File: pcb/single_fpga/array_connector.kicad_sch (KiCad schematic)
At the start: 1 part, among them J2 AXK680337YG

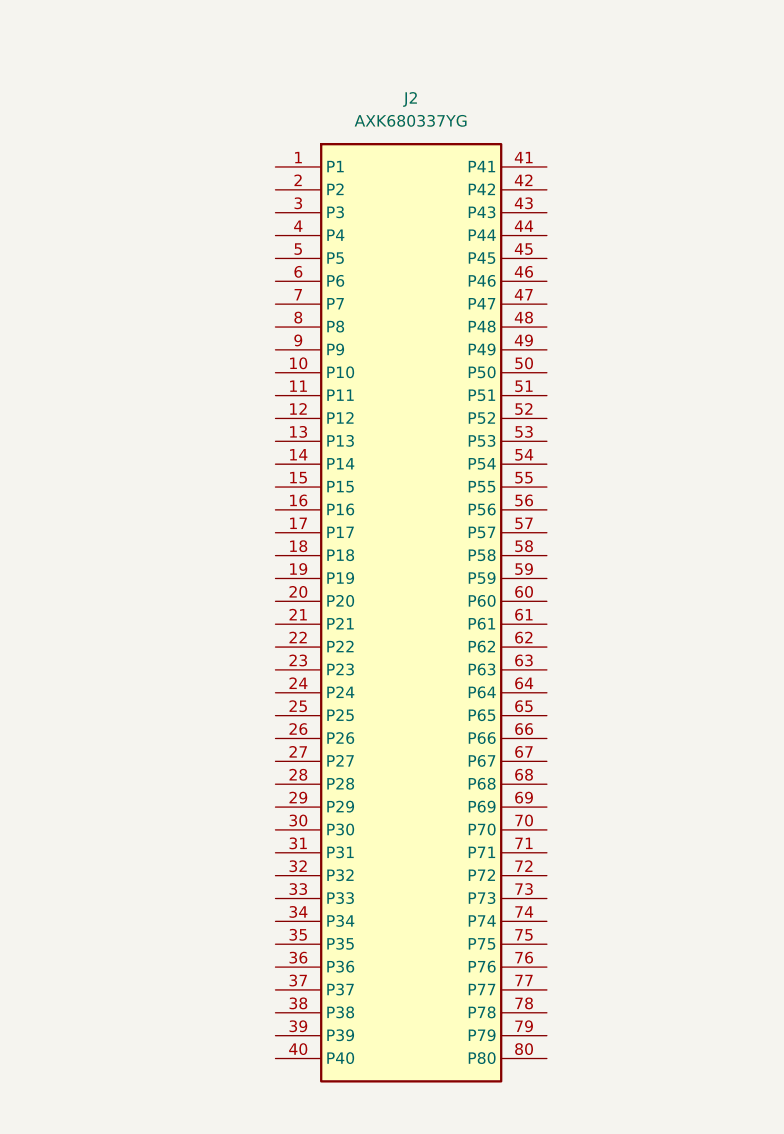
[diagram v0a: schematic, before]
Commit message: Reorganized sheets for two-boards. Fixed connector off-grid problems.
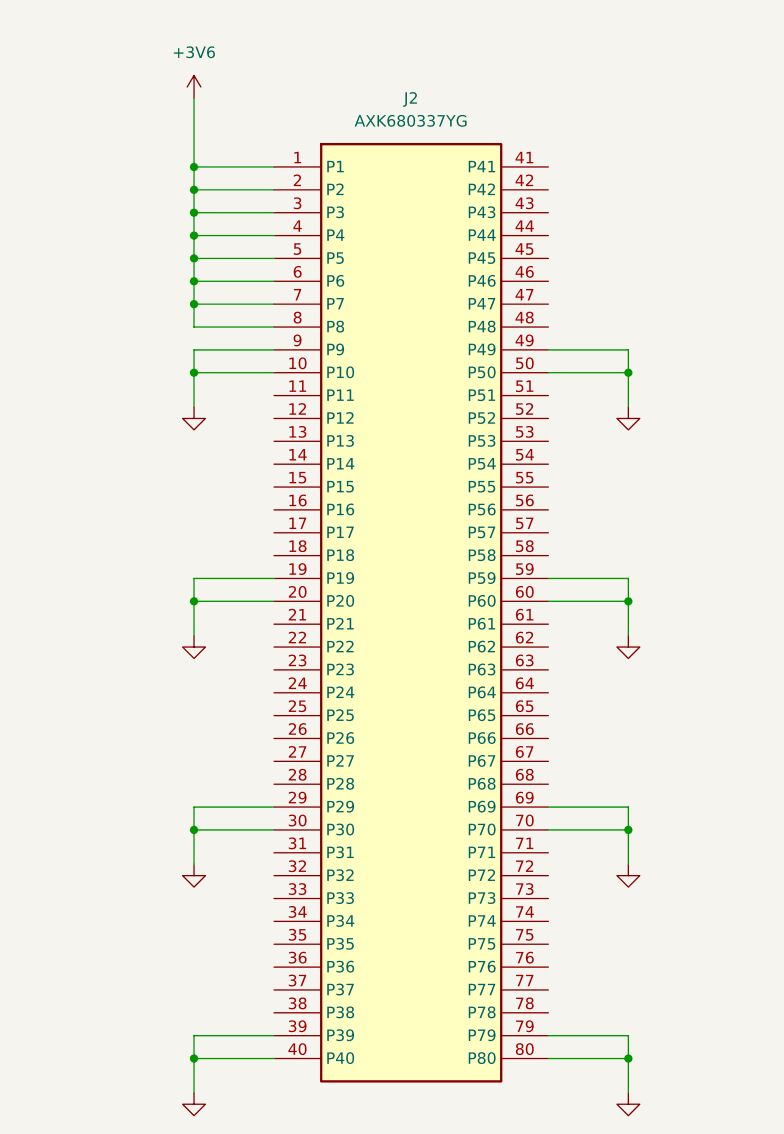
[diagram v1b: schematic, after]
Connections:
- net +3V6: now reaches J2.1 (P1)
- net +3V6: now also J2.2 (P2), J2.3 (P3), J2.4 (P4), J2.5 (P5), J2.6 (P6), J2.7 (P7), J2.8 (P8)
- net GND: now reaches J2.10 (P10)
- net GND: now also J2.19 (P19), J2.20 (P20), J2.29 (P29), J2.30 (P30), J2.39 (P39), J2.40 (P40), J2.49 (P49), J2.50 (P50), J2.59 (P59), J2.60 (P60), J2.69 (P69), J2.70 (P70), J2.79 (P79), J2.80 (P80), J2.9 (P9)

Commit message: Fixed another off-grid issue. Connected power and DATA_?? pins to inter-board connector.
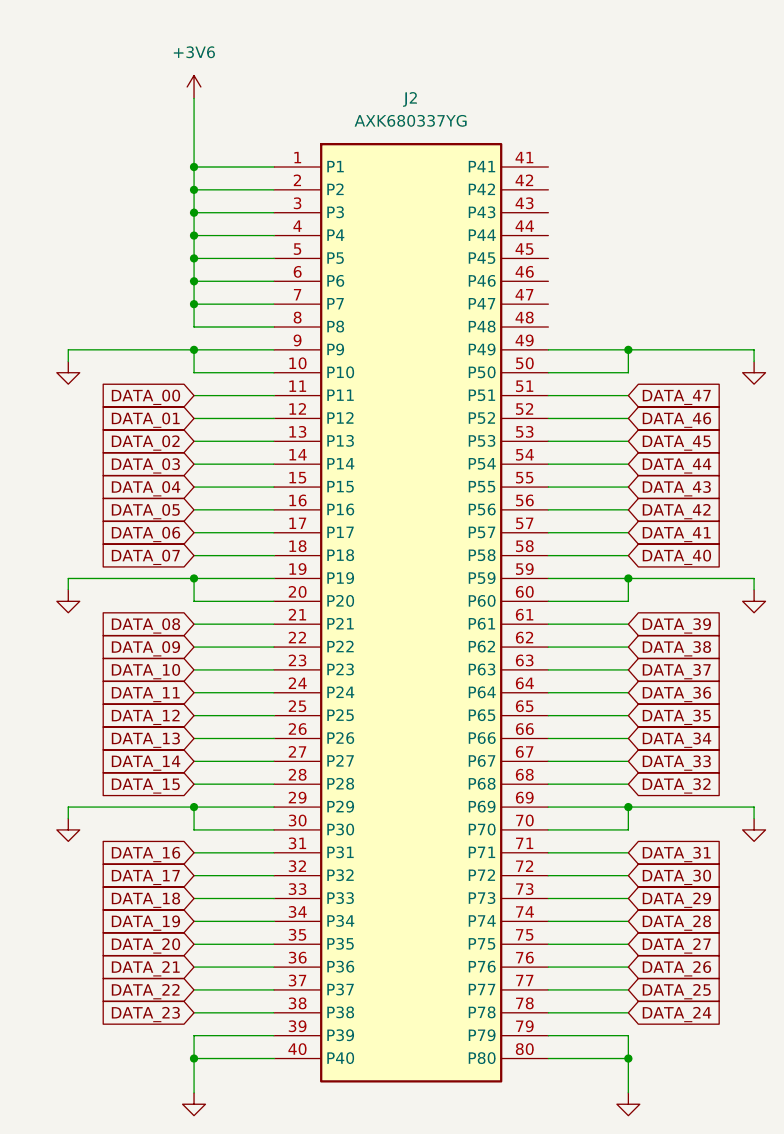
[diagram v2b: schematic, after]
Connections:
- net DATA_00: now reaches J2.11 (P11)
- net DATA_01: now reaches J2.12 (P12)
- net DATA_02: now reaches J2.13 (P13)
- net DATA_03: now reaches J2.14 (P14)
- net DATA_04: now reaches J2.15 (P15)
- net DATA_05: now reaches J2.16 (P16)
- net DATA_06: now reaches J2.17 (P17)
- net DATA_07: now reaches J2.18 (P18)
- net DATA_08: now reaches J2.21 (P21)
- net DATA_09: now reaches J2.22 (P22)
- net DATA_10: now reaches J2.23 (P23)
- net DATA_11: now reaches J2.24 (P24)
- net DATA_12: now reaches J2.25 (P25)
- net DATA_13: now reaches J2.26 (P26)
- net DATA_14: now reaches J2.27 (P27)
- net DATA_15: now reaches J2.28 (P28)
- net DATA_16: now reaches J2.31 (P31)
- net DATA_17: now reaches J2.32 (P32)
- net DATA_18: now reaches J2.33 (P33)
- net DATA_19: now reaches J2.34 (P34)
- net DATA_20: now reaches J2.35 (P35)
- net DATA_21: now reaches J2.36 (P36)
- net DATA_22: now reaches J2.37 (P37)
- net DATA_23: now reaches J2.38 (P38)
- net DATA_47: now reaches J2.51 (P51)
- net DATA_46: now reaches J2.52 (P52)
- net DATA_45: now reaches J2.53 (P53)
- net DATA_44: now reaches J2.54 (P54)
- net DATA_43: now reaches J2.55 (P55)
- net DATA_42: now reaches J2.56 (P56)
- net DATA_41: now reaches J2.57 (P57)
- net DATA_40: now reaches J2.58 (P58)
- net DATA_39: now reaches J2.61 (P61)
- net DATA_38: now reaches J2.62 (P62)
- net DATA_37: now reaches J2.63 (P63)
- net DATA_36: now reaches J2.64 (P64)
- net DATA_35: now reaches J2.65 (P65)
- net DATA_34: now reaches J2.66 (P66)
- net DATA_33: now reaches J2.67 (P67)
- net DATA_32: now reaches J2.68 (P68)
- net DATA_31: now reaches J2.71 (P71)
- net DATA_30: now reaches J2.72 (P72)
- net DATA_29: now reaches J2.73 (P73)
- net DATA_28: now reaches J2.74 (P74)
- net DATA_27: now reaches J2.75 (P75)
- net DATA_26: now reaches J2.76 (P76)
- net DATA_25: now reaches J2.77 (P77)
- net DATA_24: now reaches J2.78 (P78)

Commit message: Updated all refdes's.
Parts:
- renumbered J2 to J1
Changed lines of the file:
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@@
 		(dnp no)
 		(fields_autoplaced yes)
-		(property "Reference" "#PWR0485"
+		(property "Reference" "#PWR043"
 			(at 176.53 99.06 0)
 			(hide yes)
@@
 			(project "top"
 				(path "/12638caa-1907-413e-8e98-06abbbf6ccbc/518a49d4-764a-4074-9d90-4928dda6bfa7/a249d55d-7359-47b8-9860-fb25b30b5b2a"
-					(reference "#PWR0485")
+					(reference "#PWR043")
 					(unit 1)
 				)
@@
 		(dnp no)
 		(fields_autoplaced yes)
-		(property "Reference" "#PWR0481"
+		(property "Reference" "#PWR037"
 			(at 100.33 99.06 0)
 			(hide yes)
@@
 			(project "top"
 				(path "/12638caa-1907-413e-8e98-06abbbf6ccbc/518a49d4-764a-4074-9d90-4928dda6bfa7/a249d55d-7359-47b8-9860-fb25b30b5b2a"
-					(reference "#PWR0481")
+					(reference "#PWR037")
 					(unit 1)
 				)
@@
 		(dnp no)
 		(fields_autoplaced yes)
-		(property "Reference" "#PWR0482"
+		(property "Reference" "#PWR038"
 			(at 100.33 124.46 0)
 			(hide yes)
@@
 			(project "top"
 				(path "/12638caa-1907-413e-8e98-06abbbf6ccbc/518a49d4-764a-4074-9d90-4928dda6bfa7/a249d55d-7359-47b8-9860-fb25b30b5b2a"
-					(reference "#PWR0482")
+					(reference "#PWR038")
 					(unit 1)
 				)
@@
 		(dnp no)
 		(fields_autoplaced yes)
-		(property "Reference" "#PWR0480"
+		(property "Reference" "#PWR036"
 			(at 100.33 73.66 0)
 			(hide yes)
@@
 			(project "top"
 				(path "/12638caa-1907-413e-8e98-06abbbf6ccbc/518a49d4-764a-4074-9d90-4928dda6bfa7/a249d55d-7359-47b8-9860-fb25b30b5b2a"
-					(reference "#PWR0480")
+					(reference "#PWR036")
 					(unit 1)
 				)
@@
 		(dnp no)
 		(fields_autoplaced yes)
-		(property "Reference" "J2"
+		(property "Reference" "J1"
 			(at 138.43 38.1 0)
 			(show_name no)
@@
 			(project "top"
 				(path "/12638caa-1907-413e-8e98-06abbbf6ccbc/518a49d4-764a-4074-9d90-4928dda6bfa7/a249d55d-7359-47b8-9860-fb25b30b5b2a"
-					(reference "J2")
+					(reference "J1")
 					(unit 1)
 				)
@@
 		(dnp no)
 		(fields_autoplaced yes)
-		(property "Reference" "#PWR0483"
+		(property "Reference" "#PWR040"
 			(at 114.3 154.94 0)
 			(hide yes)
@@
 			(project "top"
 				(path "/12638caa-1907-413e-8e98-06abbbf6ccbc/518a49d4-764a-4074-9d90-4928dda6bfa7/a249d55d-7359-47b8-9860-fb25b30b5b2a"
-					(reference "#PWR0483")
+					(reference "#PWR040")
 					(unit 1)
 				)
@@
 		(dnp no)
 		(fields_autoplaced yes)
-		(property "Reference" "#PWR0486"
+		(property "Reference" "#PWR044"
 			(at 176.53 124.46 0)
 			(hide yes)
@@
 			(project "top"
 				(path "/12638caa-1907-413e-8e98-06abbbf6ccbc/518a49d4-764a-4074-9d90-4928dda6bfa7/a249d55d-7359-47b8-9860-fb25b30b5b2a"
-					(reference "#PWR0486")
+					(reference "#PWR044")
 					(unit 1)
 				)
@@
 		(dnp no)
 		(fields_autoplaced yes)
-		(property "Reference" "#PWR0484"
+		(property "Reference" "#PWR042"
 			(at 176.53 73.66 0)
 			(hide yes)
@@
 			(project "top"
 				(path "/12638caa-1907-413e-8e98-06abbbf6ccbc/518a49d4-764a-4074-9d90-4928dda6bfa7/a249d55d-7359-47b8-9860-fb25b30b5b2a"
-					(reference "#PWR0484")
+					(reference "#PWR042")
 					(unit 1)
 				)
@@
 		(dnp no)
 		(fields_autoplaced yes)
-		(property "Reference" "#PWR0495"
+		(property "Reference" "#PWR039"
 			(at 114.3 41.91 0)
 			(hide yes)
@@
 			(project "top"
 				(path "/12638caa-1907-413e-8e98-06abbbf6ccbc/518a49d4-764a-4074-9d90-4928dda6bfa7/a249d55d-7359-47b8-9860-fb25b30b5b2a"
-					(reference "#PWR0495")
+					(reference "#PWR039")
 					(unit 1)
 				)
@@
 		(dnp no)
 		(fields_autoplaced yes)
-		(property "Reference" "#PWR0487"
+		(property "Reference" "#PWR041"
 			(at 162.56 154.94 0)
 			(hide yes)
@@
 			(project "top"
 				(path "/12638caa-1907-413e-8e98-06abbbf6ccbc/518a49d4-764a-4074-9d90-4928dda6bfa7/a249d55d-7359-47b8-9860-fb25b30b5b2a"
-					(reference "#PWR0487")
+					(reference "#PWR041")
 					(unit 1)
 				)

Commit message: Changed inter-board connectors (J1 and J2) to be taller.
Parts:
- J1: value AXK680337YG -> AXK6S80347YG; footprint single_fpga:AXK680337YG -> AXK6S80347YG:CONN80_AXK6S80347YG_PAN; symbol AXK680337YG:AXK680337YG -> AXK6S80347YG:AXK6S80347YG
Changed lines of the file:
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@@
 	)
 	(symbol
-		(lib_id "AXK680337YG:AXK680337YG")
+		(lib_id "AXK6S80347YG:AXK6S80347YG")
 		(at 138.43 95.25 0)
 		(unit 1)
@@
 			)
 		)
-		(property "Value" "AXK680337YG"
+		(property "Value" "AXK6S80347YG"
 			(at 138.43 40.64 0)
 			(show_name no)
@@
 			)
 		)
-		(property "Footprint" "single_fpga:AXK680337YG"
+		(property "Footprint" "AXK6S80347YG:CONN80_AXK6S80347YG_PAN"
 			(at 138.43 95.25 0)
 			(hide yes)

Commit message: Fixed power nets.
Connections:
- no-connect marks 0 -> 8
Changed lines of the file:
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@@
 		(color 0 0 0 0)
 	)
+	(no_connect
+		(at 153.67 55.88)
+	)
+	(no_connect
+		(at 153.67 63.5)
+	)
+	(no_connect
+		(at 153.67 53.34)
+	)
+	(no_connect
+		(at 153.67 45.72)
+	)
+	(no_connect
+		(at 153.67 48.26)
+	)
+	(no_connect
+		(at 153.67 58.42)
+	)
+	(no_connect
+		(at 153.67 50.8)
+	)
+	(no_connect
+		(at 153.67 60.96)
+	)
 	(wire
 		(pts
@@
 		)
 		(instances
-			(project "top"
-				(path "/12638caa-1907-413e-8e98-06abbbf6ccbc/518a49d4-764a-4074-9d90-4928dda6bfa7/a249d55d-7359-47b8-9860-fb25b30b5b2a"
+			(project "mic_array"
+				(path "/12638caa-1907-413e-8e98-06abbbf6ccbc/a249d55d-7359-47b8-9860-fb25b30b5b2a"
 					(reference "#PWR043")
 					(unit 1)
@@
 		)
 		(instances
-			(project "top"
-				(path "/12638caa-1907-413e-8e98-06abbbf6ccbc/518a49d4-764a-4074-9d90-4928dda6bfa7/a249d55d-7359-47b8-9860-fb25b30b5b2a"
+			(project "mic_array"
+				(path "/12638caa-1907-413e-8e98-06abbbf6ccbc/a249d55d-7359-47b8-9860-fb25b30b5b2a"
 					(reference "#PWR037")
 					(unit 1)
@@
 		)
 		(instances
-			(project "top"
-				(path "/12638caa-1907-413e-8e98-06abbbf6ccbc/518a49d4-764a-4074-9d90-4928dda6bfa7/a249d55d-7359-47b8-9860-fb25b30b5b2a"
+			(project "mic_array"
+				(path "/12638caa-1907-413e-8e98-06abbbf6ccbc/a249d55d-7359-47b8-9860-fb25b30b5b2a"
 					(reference "#PWR038")
 					(unit 1)
@@
 		)
 		(instances
-			(project "top"
-				(path "/12638caa-1907-413e-8e98-06abbbf6ccbc/518a49d4-764a-4074-9d90-4928dda6bfa7/a249d55d-7359-47b8-9860-fb25b30b5b2a"
+			(project "mic_array"
+				(path "/12638caa-1907-413e-8e98-06abbbf6ccbc/a249d55d-7359-47b8-9860-fb25b30b5b2a"
 					(reference "#PWR036")
 					(unit 1)
@@
 		)
 		(instances
-			(project "top"
-				(path "/12638caa-1907-413e-8e98-06abbbf6ccbc/518a49d4-764a-4074-9d90-4928dda6bfa7/a249d55d-7359-47b8-9860-fb25b30b5b2a"
+			(project "mic_array"
+				(path "/12638caa-1907-413e-8e98-06abbbf6ccbc/a249d55d-7359-47b8-9860-fb25b30b5b2a"
 					(reference "J1")
 					(unit 1)
@@
 		)
 		(instances
-			(project "top"
-				(path "/12638caa-1907-413e-8e98-06abbbf6ccbc/518a49d4-764a-4074-9d90-4928dda6bfa7/a249d55d-7359-47b8-9860-fb25b30b5b2a"
+			(project "mic_array"
+				(path "/12638caa-1907-413e-8e98-06abbbf6ccbc/a249d55d-7359-47b8-9860-fb25b30b5b2a"
 					(reference "#PWR040")
 					(unit 1)
@@
 		)
 		(instances
-			(project "top"
-				(path "/12638caa-1907-413e-8e98-06abbbf6ccbc/518a49d4-764a-4074-9d90-4928dda6bfa7/a249d55d-7359-47b8-9860-fb25b30b5b2a"
+			(project "mic_array"
+				(path "/12638caa-1907-413e-8e98-06abbbf6ccbc/a249d55d-7359-47b8-9860-fb25b30b5b2a"
 					(reference "#PWR044")
 					(unit 1)
@@
 		)
 		(instances
-			(project "top"
-				(path "/12638caa-1907-413e-8e98-06abbbf6ccbc/518a49d4-764a-4074-9d90-4928dda6bfa7/a249d55d-7359-47b8-9860-fb25b30b5b2a"
+			(project "mic_array"
+				(path "/12638caa-1907-413e-8e98-06abbbf6ccbc/a249d55d-7359-47b8-9860-fb25b30b5b2a"
 					(reference "#PWR042")
 					(unit 1)
@@
 		)
 		(instances
-			(project "top"
-				(path "/12638caa-1907-413e-8e98-06abbbf6ccbc/518a49d4-764a-4074-9d90-4928dda6bfa7/a249d55d-7359-47b8-9860-fb25b30b5b2a"
+			(project "mic_array"
+				(path "/12638caa-1907-413e-8e98-06abbbf6ccbc/a249d55d-7359-47b8-9860-fb25b30b5b2a"
 					(reference "#PWR039")
 					(unit 1)
@@
 		)
 		(instances
-			(project "top"
-				(path "/12638caa-1907-413e-8e98-06abbbf6ccbc/518a49d4-764a-4074-9d90-4928dda6bfa7/a249d55d-7359-47b8-9860-fb25b30b5b2a"
+			(project "mic_array"
+				(path "/12638caa-1907-413e-8e98-06abbbf6ccbc/a249d55d-7359-47b8-9860-fb25b30b5b2a"
 					(reference "#PWR041")
 					(unit 1)
@@
 		)
 	)
+	(symbol
+		(lib_id "power:PWR_FLAG")
+		(at 114.3 38.1 0)
+		(mirror y)
+		(unit 1)
+		(body_style 1)
+		(exclude_from_sim no)
+		(in_bom yes)
+		(on_board yes)
+		(in_pos_files yes)
+		(dnp no)
+		(property "Reference" "#FLG03"
+			(at 114.3 33.02 0)
+			(show_name no)
+			(do_not_autoplace no)
+			(effects
+				(font
+					(size 1.27 1.27)
+				)
+			)
+		)
+		(property "Value" "PWR_FLAG"
+			(at 114.3 30.48 0)
+			(show_name no)
+			(do_not_autoplace no)
+			(effects
+				(font
+					(size 1.27 1.27)
+				)
+			)
+		)
+		(property "Footprint" ""
+			(at 114.3 38.1 0)
+			(hide yes)
+			(show_name no)
+			(do_not_autoplace no)
+			(effects
+				(font
+					(size 1.27 1.27)
+				)
+			)
+		)
+		(property "Datasheet" ""
+			(at 114.3 38.1 0)
+			(hide yes)
+			(show_name no)
+			(do_not_autoplace no)
+			(effects
+				(font
+					(size 1.27 1.27)
+				)
+			)
+		)
+		(property "Description" "Special symbol for telling ERC where power comes from -- this net is externally supplied via the board-to-board connector to the front_end board, not generated on this board."
+			(at 114.3 38.1 0)
+			(hide yes)
+			(show_name no)
+			(do_not_autoplace no)
+			(effects
+				(font
+					(size 1.27 1.27)
+				)
+			)
+		)
+		(pin "1"
+		)
+		(instances
+			(project "mic_array"
+				(path "/12638caa-1907-413e-8e98-06abbbf6ccbc/a249d55d-7359-47b8-9860-fb25b30b5b2a"
+					(reference "#FLG03")
+					(unit 1)
+				)
+			)
+		)
+	)
+	(symbol
+		(lib_id "power:PWR_FLAG")
+		(at 100.33 92.71 0)
+		(unit 1)
+		(body_style 1)
+		(exclude_from_sim no)
+		(in_bom yes)
+		(on_board yes)
+		(in_pos_files yes)
+		(dnp no)
+		(property "Reference" "#FLG04"
+			(at 100.33 87.63 0)
+			(show_name no)
+			(do_not_autoplace no)
+			(effects
+				(font
+					(size 1.27 1.27)
+				)
+			)
+		)
+		(property "Value" "PWR_FLAG"
+			(at 100.33 85.08999999999999 0)
+			(show_name no)
+			(do_not_autoplace no)
+			(effects
+				(font
+					(size 1.27 1.27)
+				)
+			)
+		)
+		(property "Footprint" ""
+			(at 100.33 92.71 0)
+			(hide yes)
+			(show_name no)
+			(do_not_autoplace no)
+			(effects
+				(font
+					(size 1.27 1.27)
+				)
+			)
+		)
+		(property "Datasheet" ""
+			(at 100.33 92.71 0)
+			(hide yes)
+			(show_name no)
+			(do_not_autoplace no)
+			(effects
+				(font
+					(size 1.27 1.27)
+				)
+			)
+		)
+		(property "Description" "Special symbol for telling ERC where power comes from -- this net is externally supplied via the board-to-board connector to the front_end board, not generated on this board."
+			(at 100.33 92.71 0)
+			(hide yes)
+			(show_name no)
+			(do_not_autoplace no)
+			(effects
+				(font
+					(size 1.27 1.27)
+				)
+			)
+		)
+		(pin "1"
+		)
+		(instances
+			(project "mic_array"
+				(path "/12638caa-1907-413e-8e98-06abbbf6ccbc/a249d55d-7359-47b8-9860-fb25b30b5b2a"
+					(reference "#FLG04")
+					(unit 1)
+				)
+			)
+		)
+	)
+	(wire
+		(pts
+			(xy 114.3 38.1) (xy 114.3 36.83)
+		)
+		(stroke
+			(width 0)
+			(type default)
+		)
+	)
+	(wire
+		(pts
+			(xy 100.33 92.71) (xy 100.33 91.44)
+		)
+		(stroke
+			(width 0)
+			(type default)
+		)
+	)
